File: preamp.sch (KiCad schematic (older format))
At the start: 19 parts, among them P1 RCA_IN, P2 Power, P3 RCA_OUT, U1 TL071

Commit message: First rev complete.
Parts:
- U1: footprint Housings_SOT-23_SOT-143_TSOT-6:SOT-23-5 -> Housings_SSOP:MSOP-8_3x3mm_Pitch0.65mm
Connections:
- net GND: now also R1.2, R2.2
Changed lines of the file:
@@
 LIBS:valves
 LIBS:custom
+LIBS:preamp-cache
 EELAYER 25 0
 EELAYER END
@@
 F 0 "U1" H 8150 5850 70  0000 C CNN
 F 1 "TL071" H 8150 5750 70  0000 C CNN
-F 2 "Housings_SOT-23_SOT-143_TSOT-6:SOT-23-5" H 8000 5550 60  0001 C CNN
+F 2 "Housings_SSOP:MSOP-8_3x3mm_Pitch0.65mm" H 8000 5550 60  0001 C CNN
 F 3 "" H 8000 5550 60  0000 C CNN
 	1    8000 5550
@@
 	1    0    0    -1
 $EndComp
+Connection ~ 5750 4900
 $EndSCHEMATC

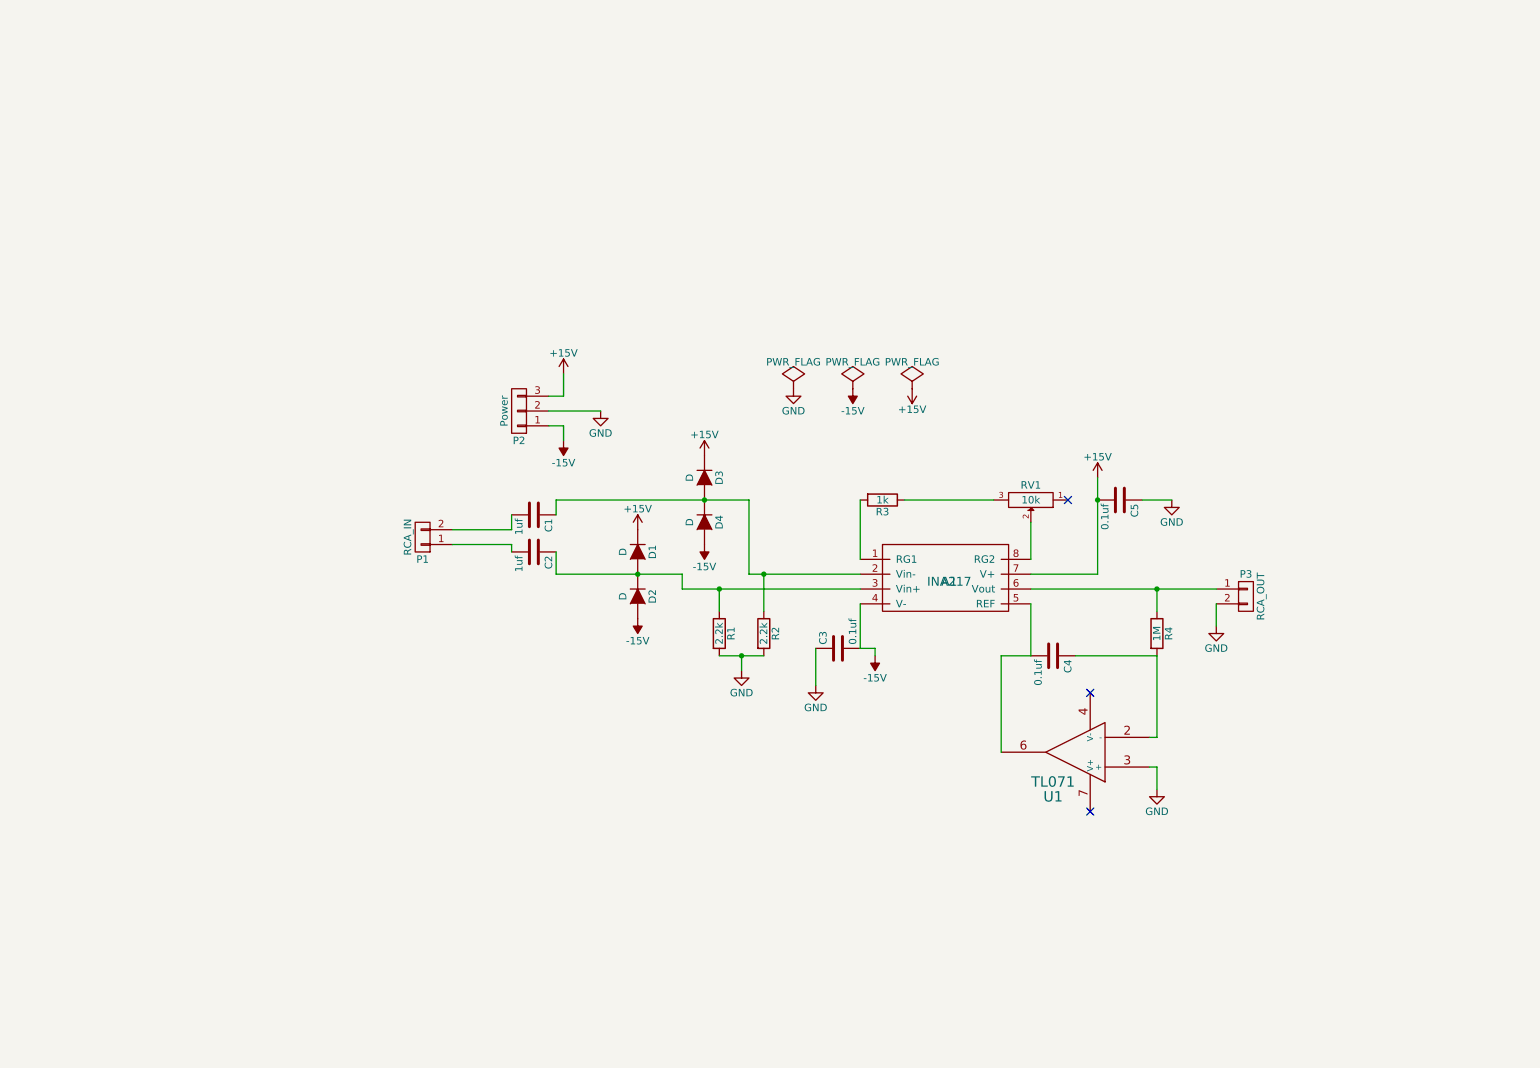
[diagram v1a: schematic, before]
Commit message: Add PSU and additional channel to schematic and parts
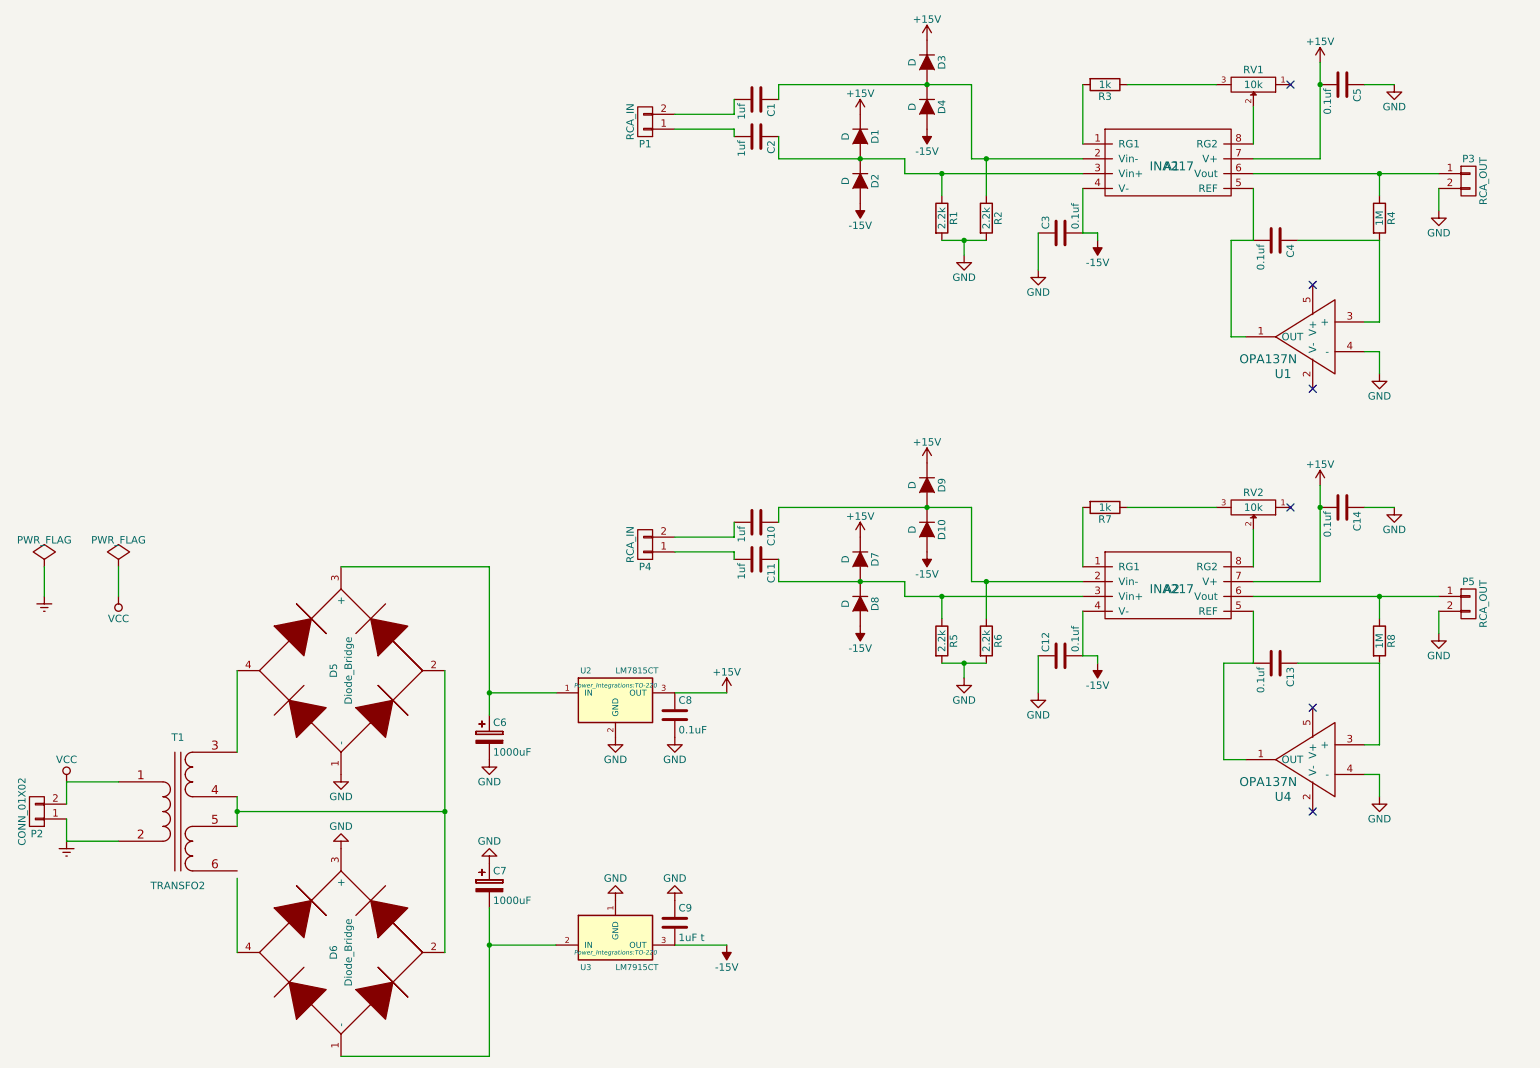
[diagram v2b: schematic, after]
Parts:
- removed P2: Power, Pin_Headers:Pin_Header_Angled_1x03, symbol CONN_01X03
- removed U1: TL071, Housings_SSOP:MSOP-8_3x3mm_Pitch0.65mm, symbol TL071
- added A2: INA217, Housings_DIP:DIP-8_W7.62mm, symbol INA217
- added C10, C11: 1uf, Capacitors_SMD:C_0805, symbol C
- added C12, C13, C14: 0.1uf, Capacitors_SMD:C_0805, symbol C
- added C6, C7: 1000uF, Capacitors_Elko_ThroughHole:Elko_vert_20x10mm_RM7.5, symbol CP
- added C8: 0.1uF, Capacitors_SMD:C_0805, symbol C
- added C9: 1uF t, Capacitors_SMD:C_0805, symbol C
- added D10, D7, D8, D9: D, Dioden_SMD_RevA_06Sep2012:Diode-Universal-SMA-SMB_Handsoldering_RevA_27July2010, symbol D
- added D5, D6: Diode_Bridge, preamp:Bridge-Rectifier-SOIC-4, symbol Diode_Bridge
- added P2: CONN_01X02, Pin_Headers:Pin_Header_Angled_1x03, symbol CONN_01X02
- added P4: RCA_IN, Pin_Headers:Pin_Header_Angled_1x02, symbol CONN_01X02
- added P5: RCA_OUT, Pin_Headers:Pin_Header_Angled_1x02, symbol CONN_01X02
- added R5, R6: 2.2k, Resistors_SMD:R_0805, symbol R
- added R7: 1k, Resistors_SMD:R_0805, symbol R
- added R8: 1M, Resistors_SMD:R_0805, symbol R
- added RV2: 10k, Potentiometers:Potentiometer_Bourns_3296W_3-8Zoll_Inline_ScrewUp, symbol POT
- added T1: TRANSFO2, preamp:preamp_transformer_6pin, symbol TRANSFO2
- added U1, U4: OPA137N, Housings_SOT-23_SOT-143_TSOT-6:SOT-23-5, symbol OPA137N
- added U2: LM7815CT, Power_Integrations:TO-220, symbol LM7815CT
- added U3: LM7915CT, Power_Integrations:TO-220, symbol LM7915CT
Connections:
- net +15V: now also A2.7 (V+), C14.2, C8.1, D7.1 (K), D9.1 (K), U2.3 (OUT)
- net -15V: now also A2.4 (V-), C12.2, C9.2, D10.2 (A), D8.2 (A), U3.3 (OUT)
- net GND: now also C12.1, C14.1, C6.2, C7.1, C8.2, C9.1, D5.1 (-), D6.3 (+), P5.2 (P2), R5.2, R6.2, U1.4 (-), U2.2 (GND), U3.1 (GND), U4.4 (-)
- net at A1.5 (REF), C4.2: now also U1.1 (OUT)
- net at C4.1, R4.2: now also U1.3 (+)
- new net: A2.1 (RG1), R7.2
- new net: A2.2 (Vin-), C10.1, D10.1 (K), D9.2 (A), R6.1
- new net: A2.3 (Vin+), C11.1, D7.2 (A), D8.1 (K), R5.1
- new net: A2.5 (REF), C13.2, U4.1 (OUT)
- new net: A2.6 (Vout), P5.1 (P1), R8.1
- new net: A2.8 (RG2), RV2.2
- new net: R7.1, RV2.3
- new net: C11.2, P4.1 (P1)
- new net: C10.2, P4.2 (P2)
- new net: C13.1, R8.2, U4.3 (+)
- new net: D5.4, T1.3 (SA)
- new net: D5.2, D6.2, T1.4 (SB), T1.5 (SC)
- new net: C6.1, D5.3 (+), U2.1 (IN)
- new net: C7.2, D6.1 (-), U3.2 (IN)
- new net Earth: P2.1 (P1), T1.2 (AB)
- new net VCC: P2.2 (P2), T1.1 (AA)
- no-connect marks 3 -> 6
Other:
- moved on the sheet: A1, C1, C2, C3, C4, C5, D1, D2, D3, D4, P1, P3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

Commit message: Expand to stereo, add AC power supply.  Not done yet.
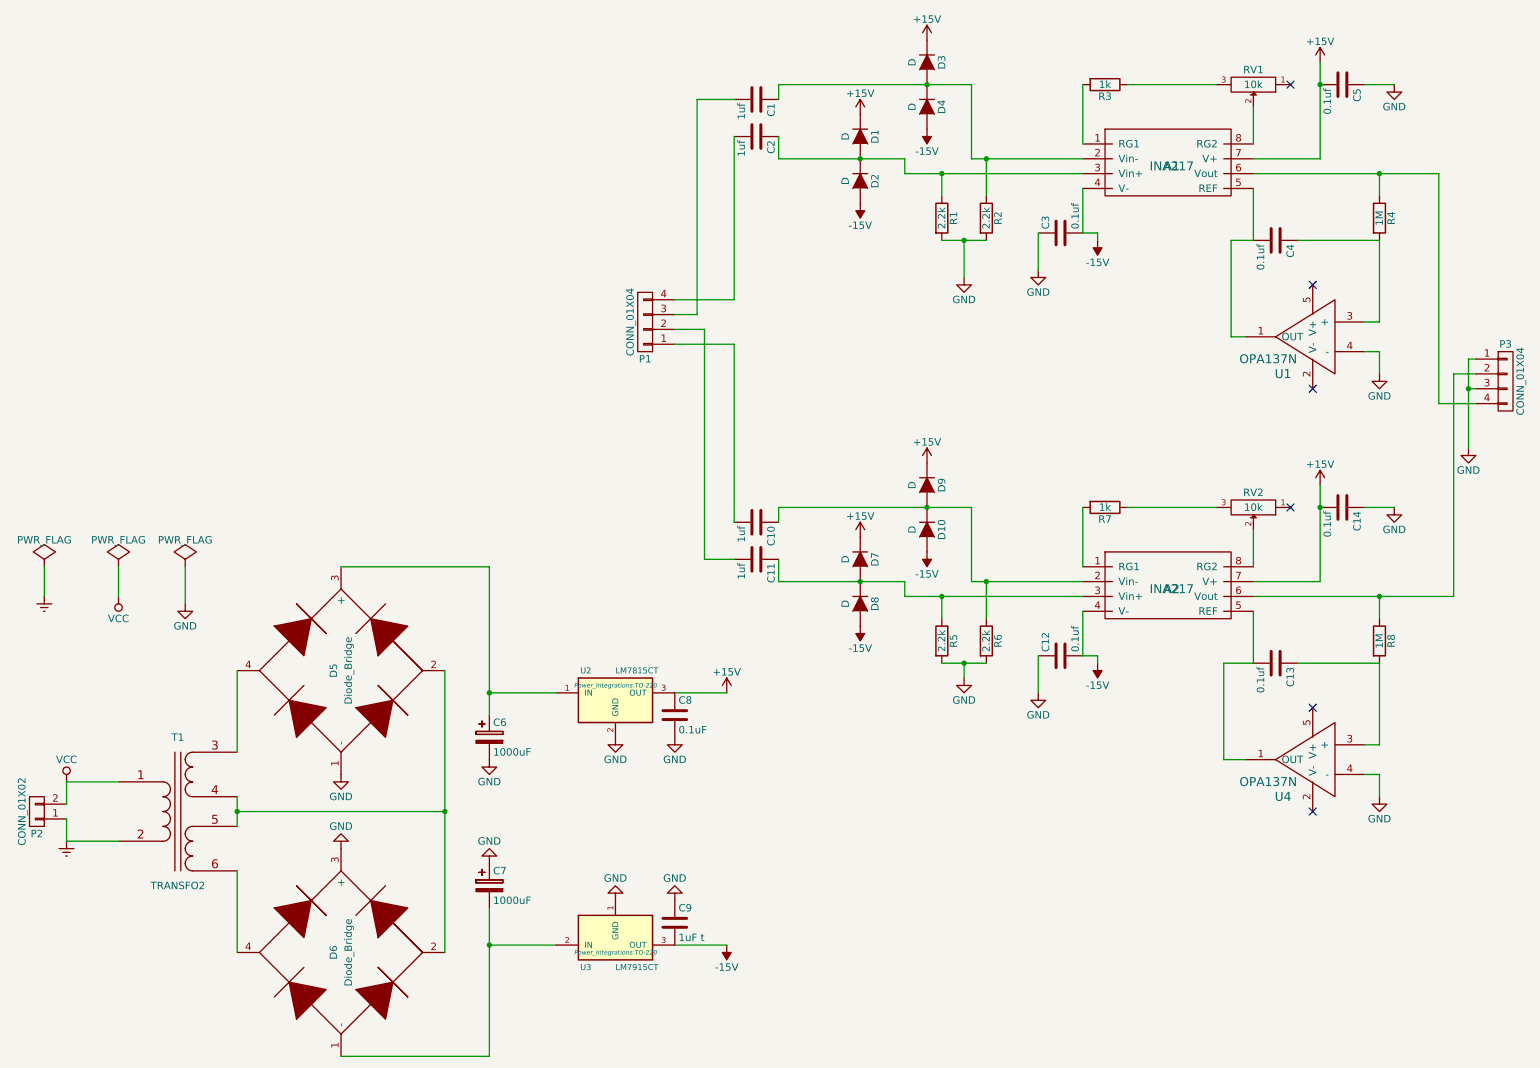
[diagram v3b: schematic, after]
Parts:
- removed P1, P4: RCA_IN, Pin_Headers:Pin_Header_Angled_1x02, symbol CONN_01X02
- removed P3, P5: RCA_OUT, Pin_Headers:Pin_Header_Angled_1x02, symbol CONN_01X02
- added P1, P3: CONN_01X04, preamp:preamp_RCA_STEREO, symbol CONN_01X04
- D1, D10, D2, D3, D4, D7, D8, D9: footprint Dioden_SMD_RevA_06Sep2012:Diode-Universal-SMA-SMB_Handsoldering_RevA_27July2010 -> Dioden_SMD_RevA_06Sep2012:Diode-SMA_Standard_RevA_26July2010
- P2: footprint Pin_Headers:Pin_Header_Angled_1x03 -> preamp:Power_Pin_Header
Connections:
- net GND: now also P3.1 (P1), P3.3 (P3)
- net at A1.6 (Vout), R4.1: now also P3.4 (P4)
- net at C2.2: now also P1.4 (P4)
- net at C1.2: now also P1.3 (P3)
- net at A2.6 (Vout), R8.1: now also P3.2 (P2)
- net at C11.2: now also P1.2 (P2)
- net at C10.2: now also P1.1 (P1)
- net at T1.6 (SD): now also D6.4
